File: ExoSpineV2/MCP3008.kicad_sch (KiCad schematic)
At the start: 15 parts, among them J15 S2B-PH-K-S(LF)(SN), J16 S2B-PH-K-S(LF)(SN), J17 S2B-PH-K-S(LF)(SN), J18 S2B-PH-K-S(LF)(SN), U4 MCP3008

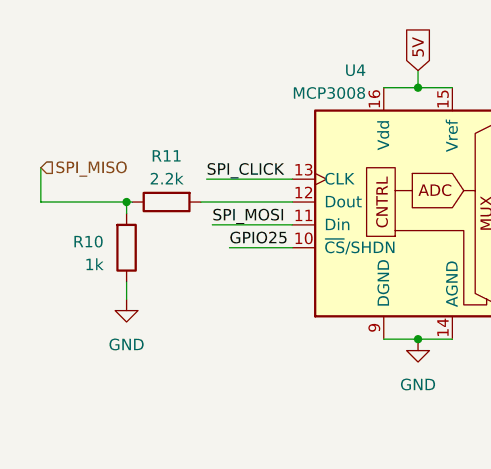
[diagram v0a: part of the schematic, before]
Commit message: created CPU circuits
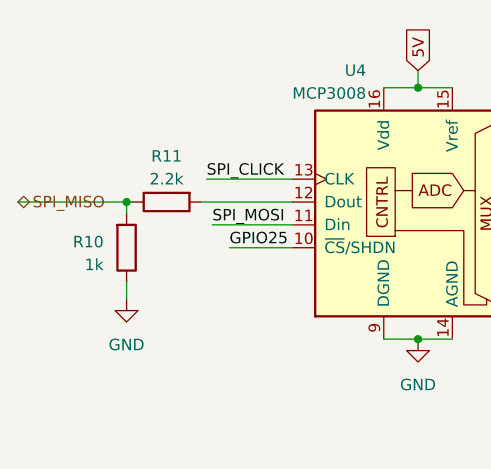
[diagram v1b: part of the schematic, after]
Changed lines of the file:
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@@
-    (stroke (width 0) (type default))
-  )
-  (wire (pts (xy 72.39 97.79) (xy 72.39 101.6))
     (stroke (width 0) (type default))
   )
@@
     (stroke (width 0) (type default))
   )
-  (wire (pts (xy 72.39 101.6) (xy 81.915 101.6))
+  (wire (pts (xy 69.85 101.6) (xy 81.915 101.6))
     (stroke (width 0) (type default))
   )
@@
     )
   )
-  (hierarchical_label "SPI_MISO" (shape input) (at 72.39 97.79 0) (fields_autoplaced)
+  (hierarchical_label "SPI_MISO" (shape bidirectional) (at 69.85 101.6 0) (fields_autoplaced)
     (effects (font (size 1.27 1.27)) (justify left))
   )

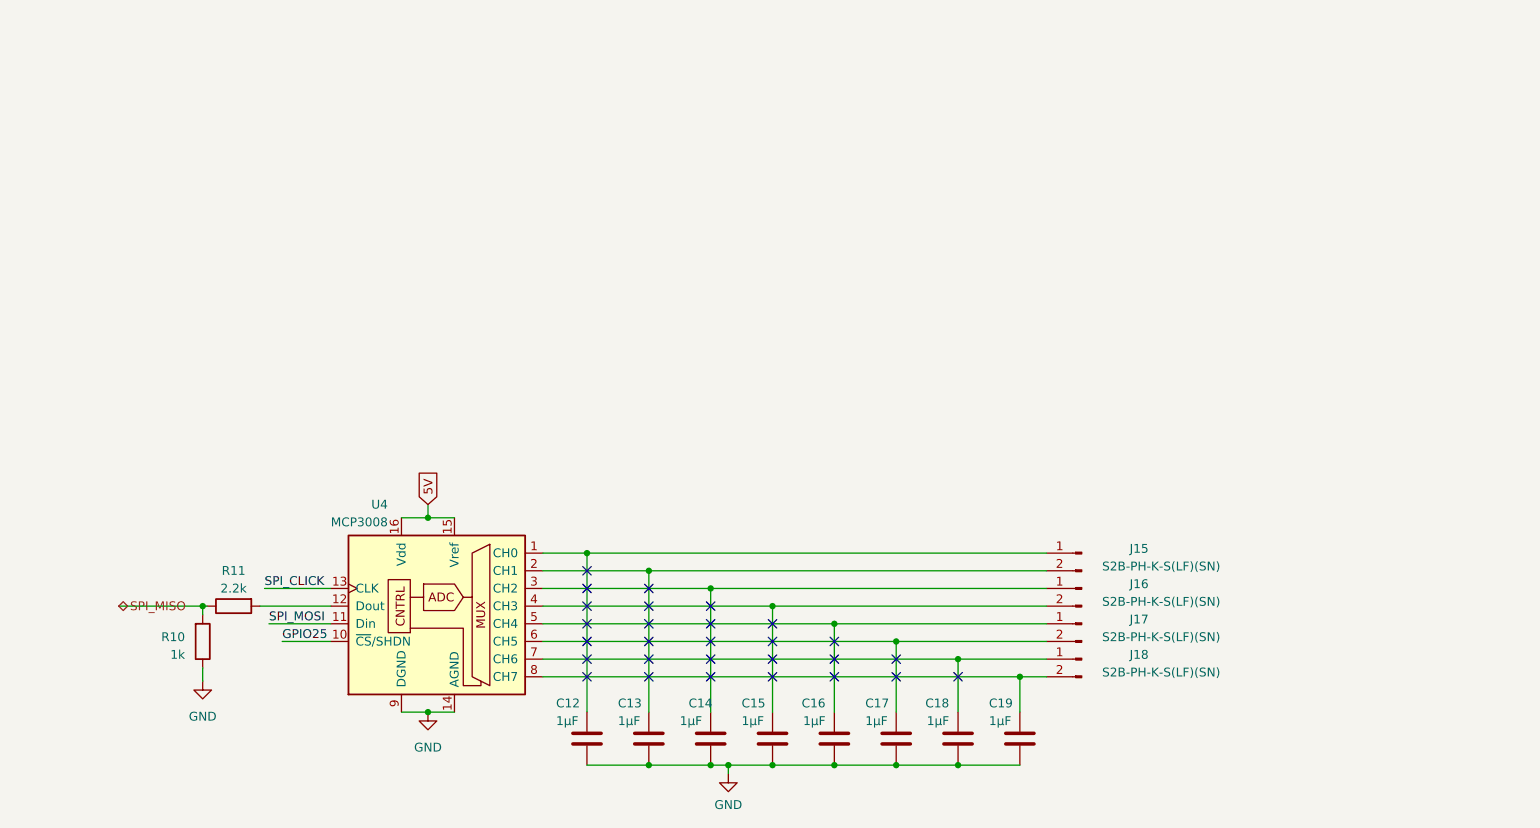
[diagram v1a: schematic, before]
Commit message: ajout des capteurs de pression (x3) et d'un peu d'info sur le dcdc12-5v
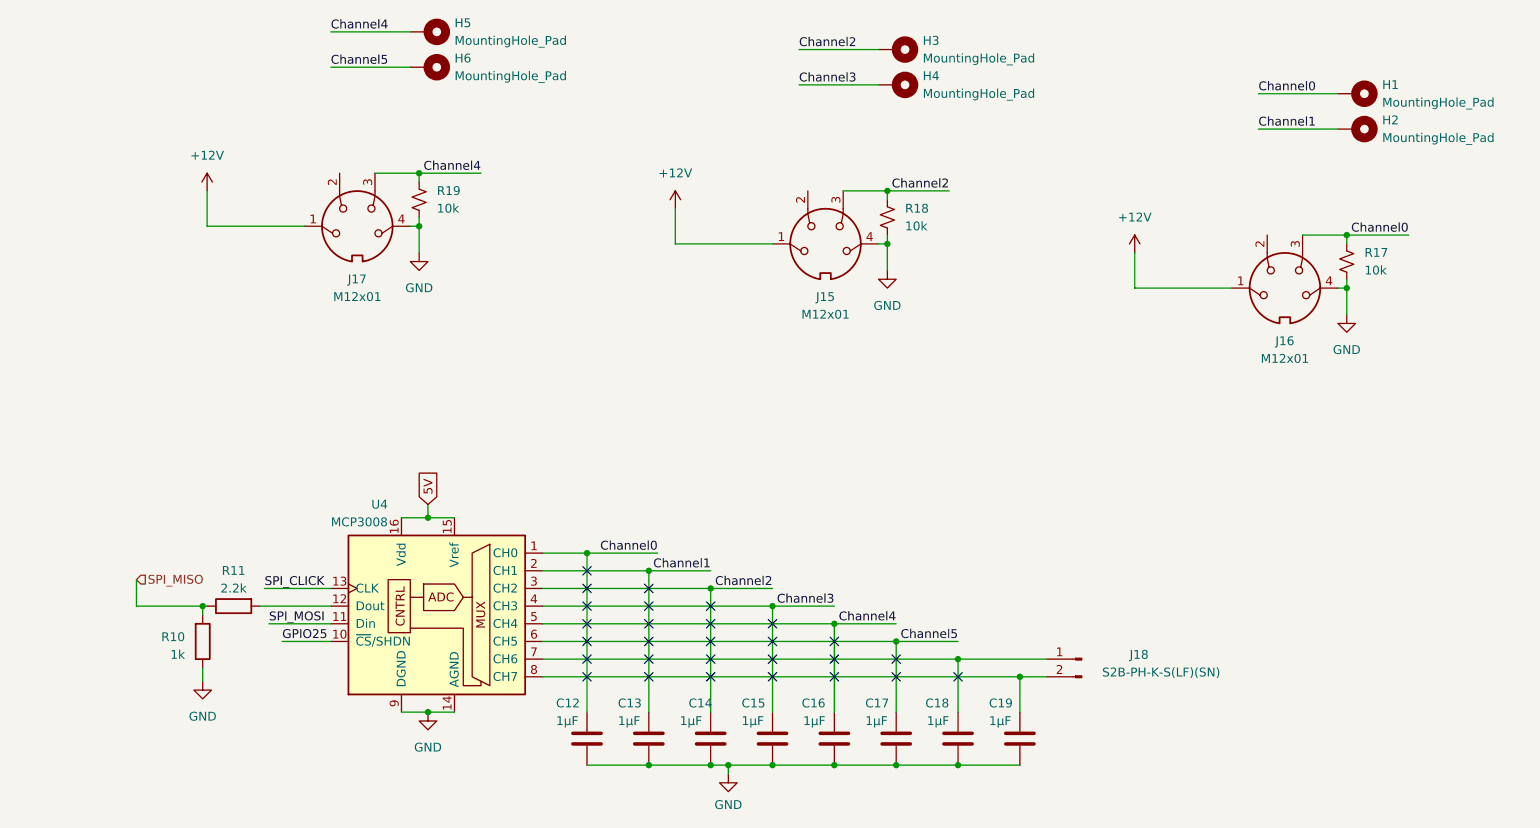
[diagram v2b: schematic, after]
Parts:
- removed J15, J16, J17: S2B-PH-K-S(LF)(SN), symbol Connector:Conn_01x02_Pin
- added H1, H2, H3, H4, H5, H6: MountingHole_Pad, symbol Mechanical:MountingHole_Pad
- added J15, J16, J17: M12x01, symbol Connector:DIN-4
- added R17, R18, R19: 10k, symbol Device:R_Small_US
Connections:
- net GND: now also J15.4, J16.4, J17.4, R17.1, R18.1, R19.1
- net Channel4: now reaches C16.1, U4.5 (CH4)
- net Channel4: now also H5.1, J17.3, R19.2
- net Channel5: now reaches C17.1, U4.6 (CH5)
- net Channel5: now also H6.1
- net Channel1: now reaches C13.1, U4.2 (CH1)
- net Channel1: now also H2.1
- net Channel0: now reaches C12.1, U4.1 (CH0)
- net Channel0: now also H1.1, J16.3, R17.2
- net Channel3: now reaches C15.1, U4.4 (CH3)
- net Channel3: now also H4.1
- net Channel2: now reaches C14.1, U4.3 (CH2)
- net Channel2: now also H3.1, J15.3, R18.2
- new net +12V: J15.1, J16.1, J17.1

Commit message: probablement pas de grandes modifications
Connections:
- net GPIO25 renamed CS/SHDN
- net SPI_CLICK renamed SPI_Click
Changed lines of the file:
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@@
+    (stroke (width 0) (type default))
+  )
+  (wire (pts (xy 90.17 110.49) (xy 90.17 104.14))
     (stroke (width 0) (type default))
   )
@@
     (stroke (width 0) (type default))
   )
+  (wire (pts (xy 90.17 104.14) (xy 100.33 104.14))
+    (stroke (width 0) (type default))
+  )
   (wire (pts (xy 233.68 33.02) (xy 245.11 33.02))
     (stroke (width 0) (type default))
@@
     (stroke (width 0) (type default))
   )
-  (wire (pts (xy 72.39 97.79) (xy 72.39 101.6))
-    (stroke (width 0) (type default))
-  )
   (wire (pts (xy 82.55 46.99) (xy 96.52 46.99))
     (stroke (width 0) (type default))
@@
     (stroke (width 0) (type default))
   )
+  (wire (pts (xy 92.71 106.68) (xy 92.71 110.49))
+    (stroke (width 0) (type default))
+  )
   (wire (pts (xy 113.03 46.99) (xy 113.03 50.8))
     (stroke (width 0) (type default))
@@
     (stroke (width 0) (type default))
   )
-  (wire (pts (xy 100.33 99.06) (xy 90.805 99.06))
-    (stroke (width 0) (type default))
-  )
   (wire (pts (xy 130.81 99.06) (xy 154.94 99.06))
     (stroke (width 0) (type default))
   )
+  (wire (pts (xy 93.98 99.06) (xy 100.33 99.06))
+    (stroke (width 0) (type default))
+  )
   (wire (pts (xy 121.92 39.37) (xy 113.03 39.37))
     (stroke (width 0) (type default))
@@
     (stroke (width 0) (type default))
   )
-  (wire (pts (xy 93.345 106.68) (xy 100.33 106.68))
+  (wire (pts (xy 92.71 106.68) (xy 100.33 106.68))
     (stroke (width 0) (type default))
   )
@@
     (stroke (width 0) (type default))
   )
-  (wire (pts (xy 91.44 104.14) (xy 100.33 104.14))
-    (stroke (width 0) (type default))
-  )
   (wire (pts (xy 246.38 55.88) (xy 246.38 54.61))
     (stroke (width 0) (type default))
@@
     (stroke (width 0) (type default))
   )
+  (wire (pts (xy 93.98 96.52) (xy 93.98 99.06))
+    (stroke (width 0) (type default))
+  )
   (wire (pts (xy 137.16 124.46) (xy 146.05 124.46))
     (stroke (width 0) (type default))
@@
     (stroke (width 0) (type default))
   )
-  (wire (pts (xy 72.39 101.6) (xy 81.915 101.6))
+  (wire (pts (xy 67.31 101.6) (xy 81.915 101.6))
     (stroke (width 0) (type default))
   )
@@
     (effects (font (size 1.27 1.27)) (justify right bottom))
   )
-  (label "GPIO25" (at 93.345 106.68 0) (fields_autoplaced)
-    (effects (font (size 1.27 1.27)) (justify left bottom))
-  )
   (label "Channel2" (at 189.23 41.91 180) (fields_autoplaced)
     (effects (font (size 1.27 1.27)) (justify right bottom))
   )
-  (label "SPI_MOSI" (at 91.44 104.14 0) (fields_autoplaced)
-    (effects (font (size 1.27 1.27)) (justify left bottom))
-  )
   (label "Channel2" (at 167.64 21.59 0) (fields_autoplaced)
     (effects (font (size 1.27 1.27)) (justify left bottom))
@@
   )
   (label "Channel3" (at 167.64 26.67 0) (fields_autoplaced)
-    (effects (font (size 1.27 1.27)) (justify left bottom))
-  )
-  (label "SPI_CLICK" (at 90.805 99.06 0) (fields_autoplaced)
     (effects (font (size 1.27 1.27)) (justify left bottom))
   )
@@
     )
   )
-  (hierarchical_label "SPI_MISO" (shape input) (at 72.39 97.79 0) (fields_autoplaced)
+  (hierarchical_label "SPI_MOSI" (shape input) (at 90.17 110.49 270) (fields_autoplaced)
+    (effects (font (size 1.27 1.27)) (justify right))
+  )
+  (hierarchical_label "CS{slash}SHDN" (shape input) (at 92.71 110.49 270) (fields_autoplaced)
+    (effects (font (size 1.27 1.27)) (justify right))
+  )
+  (hierarchical_label "SPI_Click" (shape input) (at 93.98 96.52 90) (fields_autoplaced)
     (effects (font (size 1.27 1.27)) (justify left))
   )
+  (hierarchical_label "SPI_MISO" (shape input) (at 67.31 101.6 180) (fields_autoplaced)
+    (effects (font (size 1.27 1.27)) (justify right))
+  )
   (symbol (lib_id "power:GND") (at 114.3 116.84 0) (mirror y) (unit 1)

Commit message: jsp ce que j'ai fait mais j'ai avancé
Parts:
- H1, H2: footprint (none) -> MountingHole:MountingHole_2.2mm_M2_DIN965_Pad_TopBottom
- H3: footprint (none) -> MountingHole:MountingHole_2.2mm_M2_ISO14580_Pad_TopBottom
- H4: footprint (none) -> MountingHole:MountingHole_2.7mm_M2.5_ISO7380_Pad_TopBottom
- H5: footprint (none) -> MountingHole:MountingHole_2.2mm_M2
- H6: footprint (none) -> MountingHole:MountingHole_2.2mm_M2_ISO7380_Pad_TopBottom
- J15, J16, J17: footprint (none) -> Connector_JST:JST_EH_B3B-EH-A_1x03_P2.50mm_Vertical
- J18: footprint (none) -> Connector_PinHeader_2.00mm:PinHeader_1x02_P2.00mm_Vertical
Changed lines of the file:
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@@
       (effects (font (size 1.27 1.27)) (justify left))
     )
-    (property "Footprint" "" (at 114.3 24.13 0)
+    (property "Footprint" "MountingHole:MountingHole_2.2mm_M2_ISO7380_Pad_TopBottom" (at 114.3 24.13 0)
       (effects (font (size 1.27 1.27)) hide)
     )
@@
       (effects (font (size 1.27 1.27)))
     )
-    (property "Footprint" "" (at 104.14 46.99 0)
+    (property "Footprint" "Connector_JST:JST_EH_B3B-EH-A_1x03_P2.50mm_Vertical" (at 104.14 46.99 0)
       (effects (font (size 1.27 1.27)) hide)
     )
@@
       (effects (font (size 1.27 1.27)) (justify left))
     )
-    (property "Footprint" "" (at 181.61 21.59 0)
+    (property "Footprint" "MountingHole:MountingHole_2.2mm_M2_ISO14580_Pad_TopBottom" (at 181.61 21.59 0)
       (effects (font (size 1.27 1.27)) hide)
     )
@@
       (effects (font (size 1.27 1.27)) (justify left))
     )
-    (property "Footprint" "" (at 247.65 27.94 0)
+    (property "Footprint" "MountingHole:MountingHole_2.2mm_M2_DIN965_Pad_TopBottom" (at 247.65 27.94 0)
       (effects (font (size 1.27 1.27)) hide)
     )
@@
       (effects (font (size 1.27 1.27)) (justify left))
     )
-    (property "Footprint" "" (at 114.3 19.05 0)
+    (property "Footprint" "MountingHole:MountingHole_2.2mm_M2" (at 114.3 19.05 0)
       (effects (font (size 1.27 1.27)) hide)
     )
@@
       (effects (font (size 1.27 1.27)) (justify left))
     )
-    (property "Footprint" "" (at 247.65 33.02 0)
+    (property "Footprint" "MountingHole:MountingHole_2.2mm_M2_DIN965_Pad_TopBottom" (at 247.65 33.02 0)
       (effects (font (size 1.27 1.27)) hide)
     )
@@
       (effects (font (size 1.27 1.27)))
     )
-    (property "Footprint" "" (at 237.49 55.88 0)
+    (property "Footprint" "Connector_JST:JST_EH_B3B-EH-A_1x03_P2.50mm_Vertical" (at 237.49 55.88 0)
       (effects (font (size 1.27 1.27)) hide)
     )
@@
       (effects (font (size 1.27 1.27)) (justify left))
     )
-    (property "Footprint" "" (at 181.61 26.67 0)
+    (property "Footprint" "MountingHole:MountingHole_2.7mm_M2.5_ISO7380_Pad_TopBottom" (at 181.61 26.67 0)
       (effects (font (size 1.27 1.27)) hide)
     )
@@
       (effects (font (size 1.27 1.27)))
     )
-    (property "Footprint" "" (at 208.28 109.22 0)
+    (property "Footprint" "Connector_PinHeader_2.00mm:PinHeader_1x02_P2.00mm_Vertical" (at 208.28 109.22 0)
       (effects (font (size 1.27 1.27)) hide)
     )
@@
       (effects (font (size 1.27 1.27)))
     )
-    (property "Footprint" "" (at 171.45 49.53 0)
-      (effects (font (size 1.27 1.27)) hide)
-    )
+    (property "Footprint" "Connector_JST:JST_EH_B3B-EH-A_1x03_P2.50mm_Vertical" (at 171.45 49.53 0)
+      (effects (font (size 1.27 1.27)) hide)
+    )
